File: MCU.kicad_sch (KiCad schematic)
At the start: 3 parts, among them U2 453-00001R

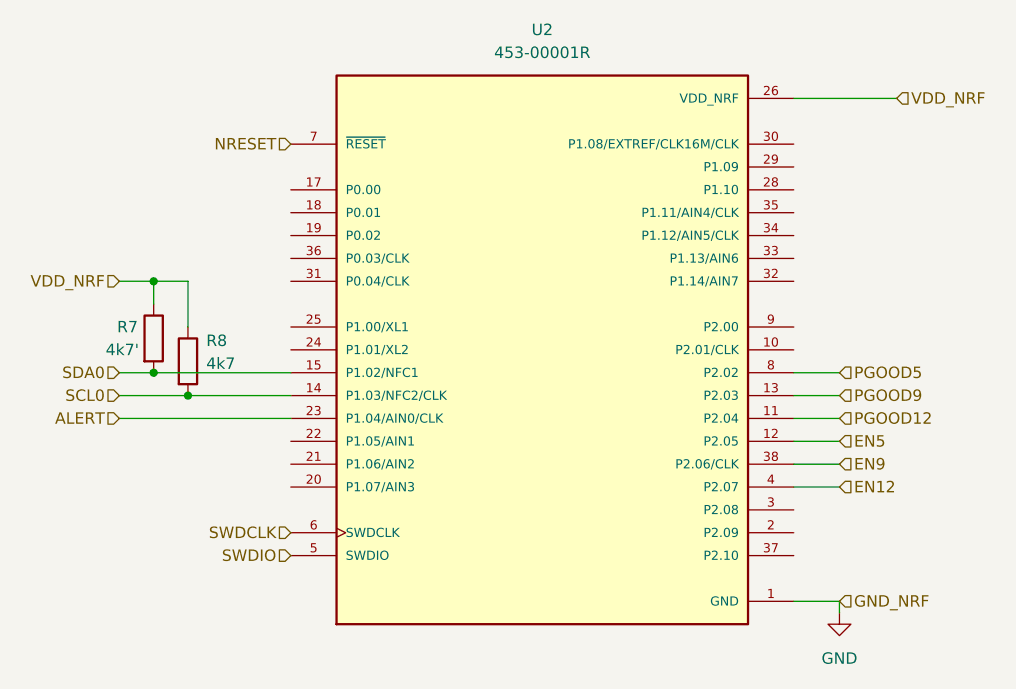
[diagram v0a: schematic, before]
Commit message: Added EN and Pgood pins for the second set of buck converters to the NRF
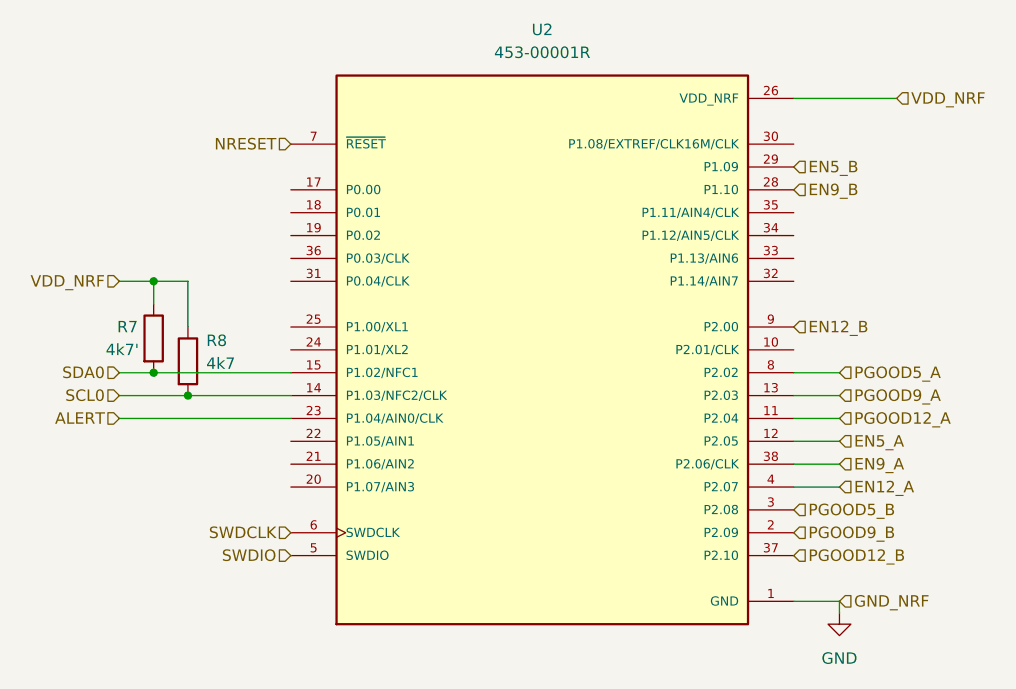
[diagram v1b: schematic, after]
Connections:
- net PGOOD9_B: now reaches U2.2 (P2.09)
- net EN9_B: now reaches U2.28 (P1.10)
- net EN5_B: now reaches U2.29 (P1.09)
- net PGOOD5_B: now reaches U2.3 (P2.08)
- net PGOOD12_B: now reaches U2.37 (P2.10)
- net EN12_B: now reaches U2.9 (P2.00)
- net EN12 renamed EN12_A
- net EN5 renamed EN5_A
- net EN9 renamed EN9_A
- net PGOOD12 renamed PGOOD12_A
- net PGOOD5 renamed PGOOD5_A
- net PGOOD9 renamed PGOOD9_A
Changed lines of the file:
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@@
+		)
+	)
+	(hierarchical_label "EN9_B"
+		(shape input)
+		(at 167.64 68.58 0)
+		(effects
+			(font
+				(size 1.27 1.27)
+			)
+			(justify left)
 		)
 	)
@@
 		)
 	)
-	(hierarchical_label "EN5"
+	(hierarchical_label "EN5_A"
 		(shape input)
 		(at 172.72 96.52 0)
@@
 		)
 	)
-	(hierarchical_label "EN12"
+	(hierarchical_label "EN5_B"
+		(shape input)
+		(at 167.64 66.04 0)
+		(effects
+			(font
+				(size 1.27 1.27)
+			)
+			(justify left)
+		)
+	)
+	(hierarchical_label "EN12_A"
 		(shape input)
 		(at 172.72 101.6 0)
@@
 		)
 	)
-	(hierarchical_label "PGOOD9"
+	(hierarchical_label "EN12_B"
+		(shape input)
+		(at 167.64 83.82 0)
+		(effects
+			(font
+				(size 1.27 1.27)
+			)
+			(justify left)
+		)
+	)
+	(hierarchical_label "PGOOD9_B"
+		(shape input)
+		(at 167.64 106.68 0)
+		(effects
+			(font
+				(size 1.27 1.27)
+			)
+			(justify left)
+		)
+	)
+	(hierarchical_label "PGOOD12_B"
+		(shape input)
+		(at 167.64 109.22 0)
+		(effects
+			(font
+				(size 1.27 1.27)
+			)
+			(justify left)
+		)
+	)
+	(hierarchical_label "PGOOD9_A"
 		(shape input)
 		(at 172.72 91.44 0)
@@
 		)
 	)
-	(hierarchical_label "EN9"
+	(hierarchical_label "EN9_A"
 		(shape input)
 		(at 172.72 99.06 0)
@@
 		)
 	)
-	(hierarchical_label "PGOOD12"
+	(hierarchical_label "PGOOD12_A"
 		(shape input)
 		(at 172.72 93.98 0)
@@
 		)
 	)
-	(hierarchical_label "PGOOD5"
+	(hierarchical_label "PGOOD5_A"
 		(shape input)
 		(at 172.72 88.9 0)
 		(effects
 			(font
+				(size 1.27 1.27)
+			)
+			(justify left)
+		)
+	)
+	(hierarchical_label "PGOOD5_B"
+		(shape input)
+		(at 167.64 104.14 0)
+		(effects
+			(font
